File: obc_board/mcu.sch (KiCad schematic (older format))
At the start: 35 parts

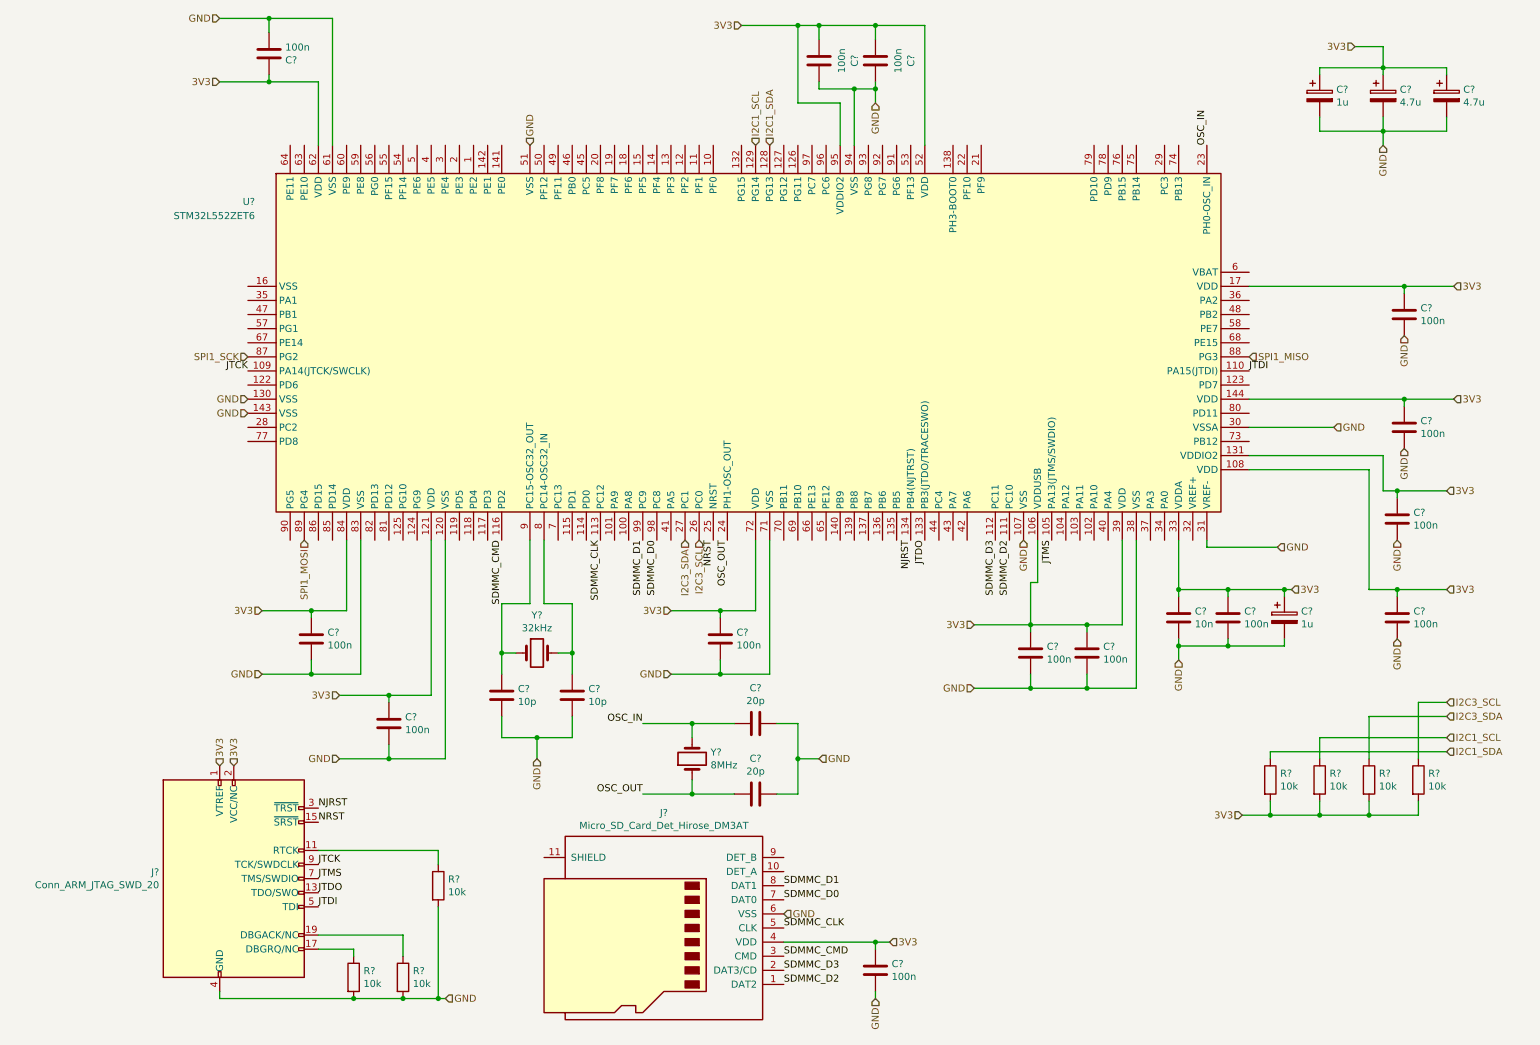
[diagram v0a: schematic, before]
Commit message: add memory
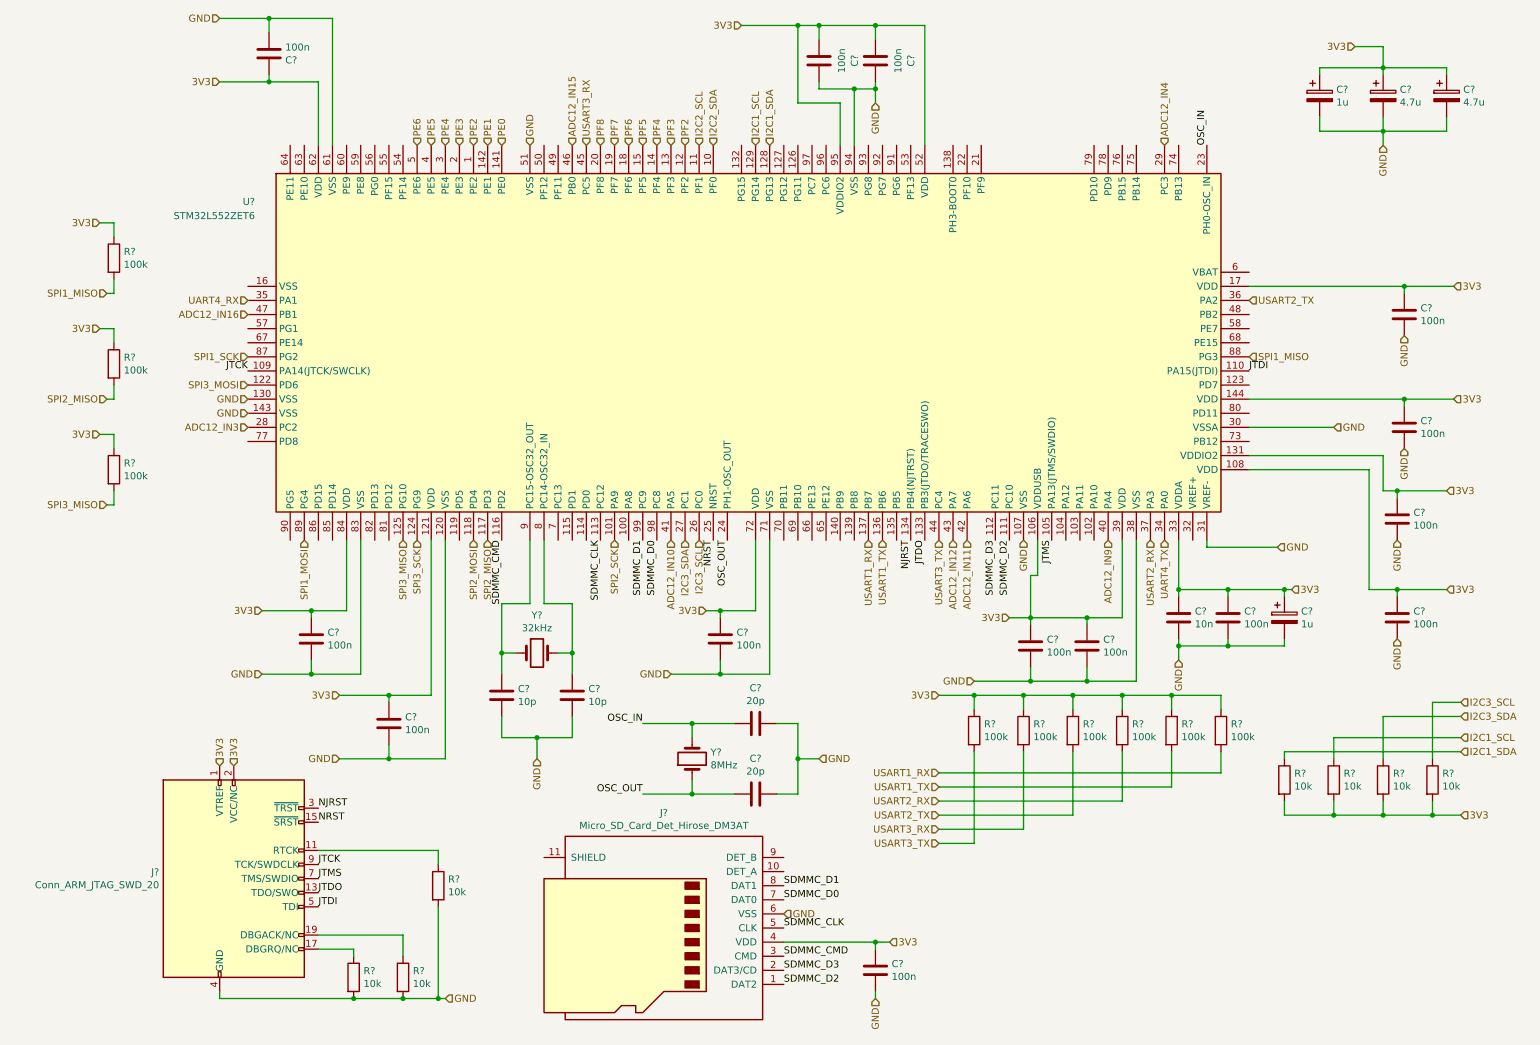
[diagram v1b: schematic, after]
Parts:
- added R? (x9): 100k, symbol Device:R
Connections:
- net 3V3: now also R?.1, R?.1, R?.1, R?.1, R?.1, R?.1, R?.1, R?.1, R?.1
- net SPI1_MISO: now also R?.2
- net PE2: now reaches U?.1 (PE2)
- net I2C2_SDA: now reaches U?.10 (PF0)
- net SPI2_SCK: now reaches U?.101 (PA9)
- net I2C2_SCL: now reaches U?.11 (PF1)
- net SPI2_MISO: now reaches U?.117 (PD3)
- net SPI2_MISO: now also R?.2
- net SPI2_MOSI: now reaches U?.118 (PD4)
- net PF2: now reaches U?.12 (PF2)
- net SPI3_MOSI: now reaches U?.122 (PD6)
- net SPI3_SCK: now reaches U?.124 (PG9)
- net SPI3_MISO: now reaches U?.125 (PG10)
- net SPI3_MISO: now also R?.2
- net PF3: now reaches U?.13 (PF3)
- net USART1_TX: now reaches U?.136 (PB6)
- net USART1_TX: now also R?.2
- net USART1_RX: now reaches U?.137 (PB7)
- net USART1_RX: now also R?.2
- net PF4: now reaches U?.14 (PF4)
- net PE0: now reaches U?.141 (PE0)
- net PE1: now reaches U?.142 (PE1)
- net PF5: now reaches U?.15 (PF5)
- net PF6: now reaches U?.18 (PF6)
- net PF7: now reaches U?.19 (PF7)
- net PE3: now reaches U?.2 (PE3)
- net PF8: now reaches U?.20 (PF8)
- net ADC12_IN3: now reaches U?.28 (PC2)
- net ADC12_IN4: now reaches U?.29 (PC3)
- net PE4: now reaches U?.3 (PE4)
- net UART4_TX: now reaches U?.34 (PA0)
- net UART4_RX: now reaches U?.35 (PA1)
- net USART2_TX: now reaches U?.36 (PA2)
- net USART2_TX: now also R?.2
- net USART2_RX: now reaches U?.37 (PA3)
- net USART2_RX: now also R?.2
- net PE5: now reaches U?.4 (PE5)
- net ADC12_IN9: now reaches U?.40 (PA4)
- net ADC12_IN10: now reaches U?.41 (PA5)
- net ADC12_IN11: now reaches U?.42 (PA6)
- net ADC12_IN12: now reaches U?.43 (PA7)
- net USART3_TX: now reaches U?.44 (PC4)
- net USART3_TX: now also R?.2
- net USART3_RX: now reaches U?.45 (PC5)
- net USART3_RX: now also R?.2
- net ADC12_IN15: now reaches U?.46 (PB0)
- net ADC12_IN16: now reaches U?.47 (PB1)
- net PE6: now reaches U?.5 (PE6)
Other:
- moved on the sheet: C?, R?

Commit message: updated footprints
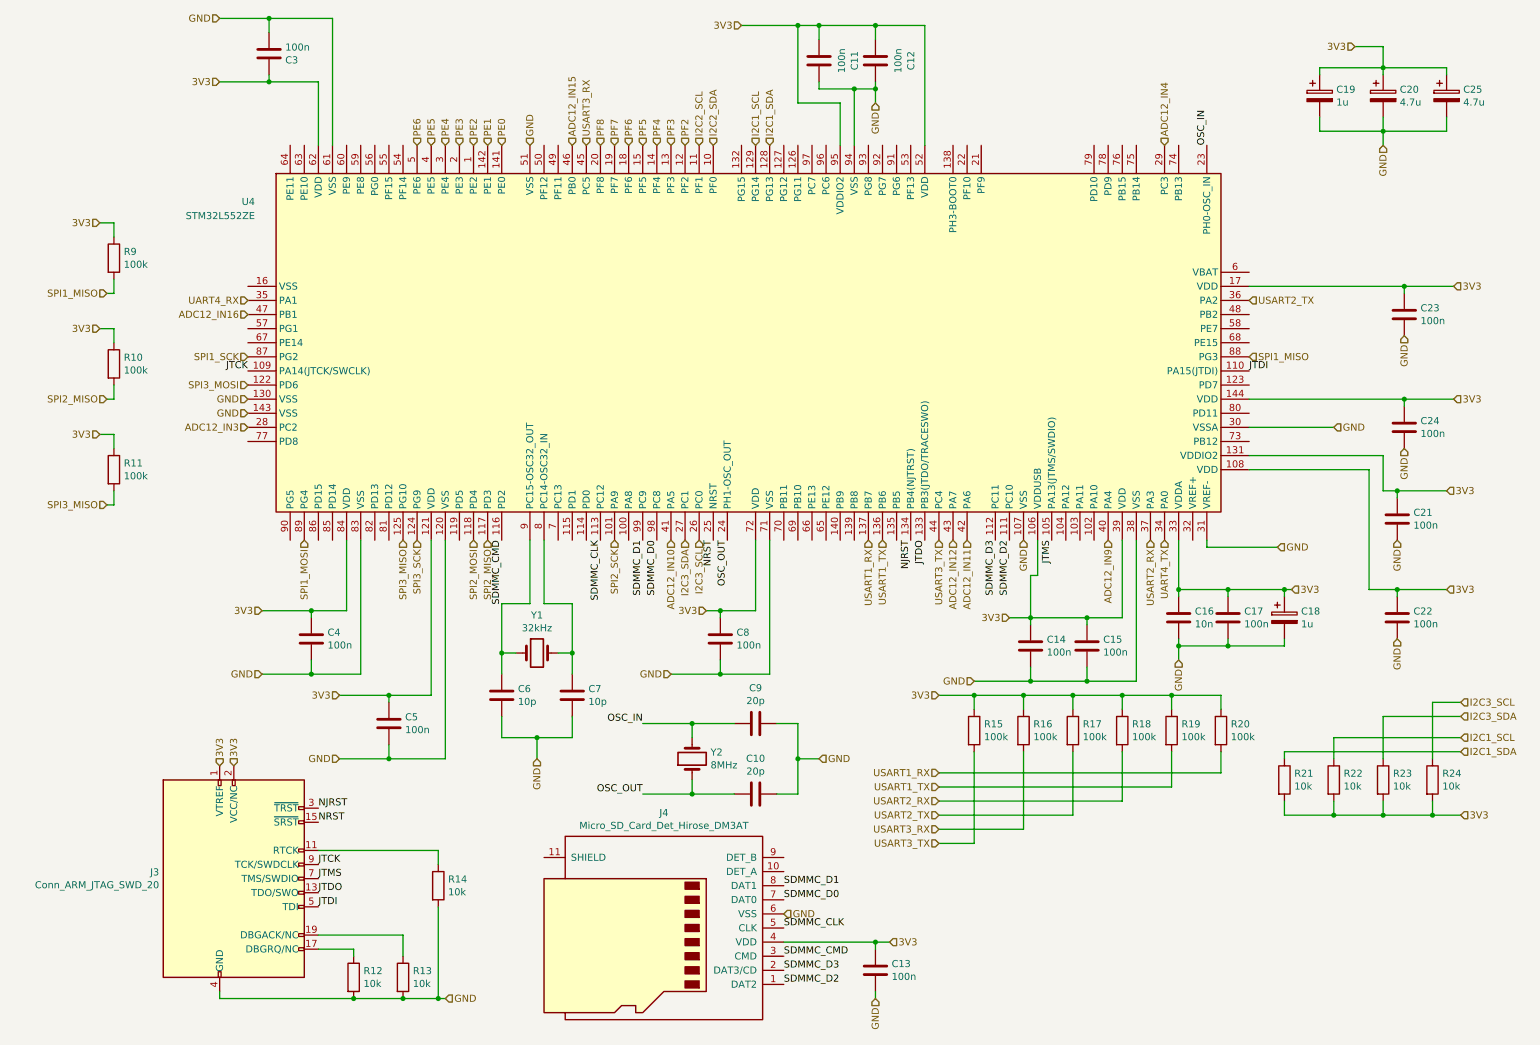
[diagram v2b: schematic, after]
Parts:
- C11, C12, C13, C14, C15, C17, C21, C22, C23, C24, C3, C4, C5, C8: renamed from C?; footprint (none) -> cubesat_obc:CAPC1005X55N; Digikey Part Number (none) -> 490-13342-1-ND
- C16: renamed from C?; footprint (none) -> cubesat_obc:CAPC0603X33N; Digikey Part Number (none) -> 490-6143-1-ND
- U4: renamed from U?; value STM32L552ZET6 -> STM32L552ZE; footprint Package_QFP:LQFP-144_20x20mm_P0.5mm -> cubesat_obc:LQFP-144_20x20mm_P0.5mm; Digikey Part Number (none) -> 497-STM32L552ZET6-ND
- gave numbers to parts that had none: 28

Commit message: footprints
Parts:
- C10, C9: footprint (none) -> Capacitor_SMD:C_0201_0603Metric; Digikey Part Number (none) -> 490-9618-1-ND
- C11, C12, C13, C14, C15, C17, C21, C22, C23, C24, C3, C4, C5, C8: footprint cubesat_obc:CAPC1005X55N -> Capacitor_SMD:C_0402_1005Metric; Digikey Part Number 490-13342-1-ND -> 490-16433-1-ND
- C16: footprint cubesat_obc:CAPC0603X33N -> Capacitor_SMD:C_0805_2012Metric; Digikey Part Number 490-6143-1-ND -> 490-8295-1-ND
- C18, C19: footprint (none) -> Capacitor_THT:CP_Radial_D5.0mm_P2.00mm; Digikey Part Number (none) -> 493-15407-ND
- C20, C25: footprint (none) -> Capacitor_THT:CP_Radial_D5.0mm_P2.00mm; Digikey Part Number (none) -> 493-15371-ND
- C6, C7: footprint (none) -> Capacitor_SMD:C_0201_0603Metric; Digikey Part Number (none) -> 490-7750-1-ND
- J3: footprint (none) -> Connector_IDC:IDC-Header_2x10_P2.54mm_Vertical
- J4: footprint (none) -> cubesat_obc:HRS_DM3AT-SF-PEJM5; Digikey Part Number (none) -> HR1964CT-ND
- R10, R11, R15, R16, R17, R18, R19, R20, R9: footprint (none) -> Resistor_SMD:R_0402_1005Metric; Digikey Part Number (none) -> 311-100KLRCT-ND
- R12, R13, R14, R21, R22, R23, R24: footprint (none) -> Resistor_SMD:R_0402_1005Metric; Digikey Part Number (none) -> 311-10.0KLRCT-ND

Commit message: expose more ios
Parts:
- removed J3: Conn_ARM_JTAG_SWD_20, Connector_IDC:IDC-Header_2x10_P2.54mm_Vertical, symbol Connector:Conn_ARM_JTAG_SWD_20
- removed J4: Micro_SD_Card_Det_Hirose_DM3AT, cubesat_obc:HRS_DM3AT-SF-PEJM5, symbol Connector:Micro_SD_Card_Det_Hirose_DM3AT
- removed R12, R13, R14: 10k, Resistor_SMD:R_0402_1005Metric, symbol Device:R
- added J4: Micro_SD_Card, cubesat_obc:microSD_HC_Wuerth_693072010801, symbol Connector:Micro_SD_Card
- added J?: Conn_01x08_Female, symbol Connector:Conn_01x08_Female
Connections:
- net 3V3: now also J?.8 (Pin_8)
- net GND: now also J4.6 (VSS), J4.9 (SHIELD), J?.7 (Pin_7)
- net JTCK: now also J?.4 (Pin_4)
- net JTDI: now also J?.1 (Pin_1)
- net JTDO: now also J?.2 (Pin_2)
- net JTMS: now also J?.3 (Pin_3)
- net NJRST: now also J?.6 (Pin_6)
- net NRST: now also J?.5 (Pin_5)
- net SDMMC_CLK: now also J4.5 (CLK)
- net SDMMC_CMD: now also J4.3 (CMD)
- net SDMMC_D0: now also J4.7 (DAT0)
- net SDMMC_D1: now also J4.8 (DAT1)
- net SDMMC_D2: now also J4.1 (DAT2)
- net SDMMC_D3: now also J4.2 (DAT3/CD)
- net 3V3_P: now reaches U4.6 (VBAT)
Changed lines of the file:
@@
 $Descr A4 11693 8268
 encoding utf-8
-Sheet 3 5
+Sheet 3 6
 Title ""
 Date ""
@@
 Wire Wire Line
 	5250 6100 5550 6100
-$Comp
-L Connector:Conn_ARM_JTAG_SWD_20 J3
-U 1 1 5E8B9B17
-P 2000 6700
-F 0 "J3" H 1471 6746 50  0000 R CNN
-F 1 "Conn_ARM_JTAG_SWD_20" H 1471 6655 50  0000 R CNN
-F 2 "Connector_IDC:IDC-Header_2x10_P2.54mm_Vertical" H 2450 5650 50  0001 L TNN
-F 3 "http://infocenter.arm.com/help/topic/com.arm.doc.dui0499b/DUI0499B_system_design_reference.pdf" V 1650 5450 50  0001 C CNN
-	1    2000 6700
-	1    0    0    -1
-$EndComp
-Text HLabel 1900 5900 1    50   Input ~ 0
-3V3
-Text HLabel 2000 5900 1    50   Input ~ 0
-3V3
-Text HLabel 3500 7550 2    50   Input ~ 0
-GND
-Wire Wire Line
-	1900 7550 1900 7500
-Wire Wire Line
-	1900 7550 2850 7550
-$Comp
-L Device:R R12
-U 1 1 5E922293
-P 2850 7400
-F 0 "R12" H 2920 7446 50  0000 L CNN
-F 1 "10k" H 2920 7355 50  0000 L CNN
-F 2 "Resistor_SMD:R_0402_1005Metric" V 2780 7400 50  0001 C CNN
-F 3 "https://www.yageo.com/upload/media/product/productsearch/datasheet/rchip/PYu-RC_Group_51_RoHS_L_11.pdf~" H 2850 7400 50  0001 C CNN
-F 4 "311-10.0KLRCT-ND" H 2850 7400 50  0001 C CNN "Digikey Part Number"
-	1    2850 7400
-	1    0    0    -1
-$EndComp
-Connection ~ 2850 7550
-Wire Wire Line
-	2850 7550 3200 7550
-$Comp
-L Device:R R13
-U 1 1 5E922EFC
-P 3200 7400
-F 0 "R13" H 3270 7446 50  0000 L CNN
-F 1 "10k" H 3270 7355 50  0000 L CNN
-F 2 "Resistor_SMD:R_0402_1005Metric" V 3130 7400 50  0001 C CNN
-F 3 "https://www.yageo.com/upload/media/product/productsearch/datasheet/rchip/PYu-RC_Group_51_RoHS_L_11.pdf~" H 3200 7400 50  0001 C CNN
-F 4 "311-10.0KLRCT-ND" H 3200 7400 50  0001 C CNN "Digikey Part Number"
-	1    3200 7400
-	1    0    0    -1
-$EndComp
-Wire Wire Line
-	2600 7200 2850 7200
-Wire Wire Line
-	2850 7200 2850 7250
-$Comp
-L Device:R R14
-U 1 1 5E92F679
-P 3450 6750
-F 0 "R14" H 3520 6796 50  0000 L CNN
-F 1 "10k" H 3520 6705 50  0000 L CNN
-F 2 "Resistor_SMD:R_0402_1005Metric" V 3380 6750 50  0001 C CNN
-F 3 "https://www.yageo.com/upload/media/product/productsearch/datasheet/rchip/PYu-RC_Group_51_RoHS_L_11.pdf~" H 3450 6750 50  0001 C CNN
-F 4 "311-10.0KLRCT-ND" H 3450 6750 50  0001 C CNN "Digikey Part Number"
-	1    3450 6750
-	1    0    0    -1
-$EndComp
-Connection ~ 3200 7550
-Wire Wire Line
-	3200 7550 3450 7550
-Wire Wire Line
-	3200 7250 3200 7100
-Wire Wire Line
-	3200 7100 2600 7100
-Wire Wire Line
-	3450 6900 3450 7550
-Connection ~ 3450 7550
-Wire Wire Line
-	3450 7550 3500 7550
-Wire Wire Line
-	3450 6600 3450 6500
-Wire Wire Line
-	3450 6500 2600 6500
+Text HLabel 1800 6500 2    50   Input ~ 0
+3V3
 Text HLabel 8700 5150 3    50   Input ~ 0
 GND
@@
 Text Label 4900 6100 2    50   ~ 0
 OSC_OUT
-Text Label 2600 6900 0    50   ~ 0
+Text Label 1800 7200 0    50   ~ 0
 JTDI
-Text Label 2600 6800 0    50   ~ 0
+Text Label 1800 7100 0    50   ~ 0
 JTDO
-Text Label 2600 6700 0    50   ~ 0
+Text Label 1800 7000 0    50   ~ 0
 JTMS
-Text Label 2600 6600 0    50   ~ 0
+Text Label 1800 6900 0    50   ~ 0
 JTCK
-Text Label 2600 6200 0    50   ~ 0
+Text Label 1800 6700 0    50   ~ 0
 NJRST
-Text Label 2600 6300 0    50   ~ 0
+Text Label 1800 6800 0    50   ~ 0
 NRST
 Wire Wire Line
@@
 Text HLabel 5200 4300 3    50   Input ~ 0
 I2C3_SDA
-$Comp
-L Connector:Micro_SD_Card_Det_Hirose_DM3AT J4
-U 1 1 5F6001BE
-P 5000 7050
-F 0 "J4" H 4950 6233 50  0000 C CNN
-F 1 "Micro_SD_Card_Det_Hirose_DM3AT" H 4950 6324 50  0000 C CNN
-F 2 "cubesat_obc:HRS_DM3AT-SF-PEJM5" H 7050 7750 50  0001 C CNN
-F 3 "https://www.hirose.com/product/document?clcode=CL0609-0033-6-00&productname=DM3AT-SF-PEJ2M5&series=DM3&documenttype=Catalog&lang=en&documentid=D49662_en" H 5000 7150 50  0001 C CNN
-F 4 "HR1964CT-ND" H 5000 7050 50  0001 C CNN "Digikey Part Number"
-	1    5000 7050
-	-1   0    0    1
-$EndComp
 Connection ~ 2250 600
 Wire Wire Line
@@
 Text Label 4600 4300 3    50   ~ 0
 SDMMC_CLK
-Text Label 5900 6850 0    50   ~ 0
+Text Label 4550 6700 0    50   ~ 0
 SDMMC_D0
-Text Label 5900 6750 0    50   ~ 0
+Text Label 4550 6600 0    50   ~ 0
 SDMMC_D1
-Text Label 5900 7450 0    50   ~ 0
+Text Label 4550 7300 0    50   ~ 0
 SDMMC_D2
-Text Label 5900 7350 0    50   ~ 0
+Text Label 4550 7200 0    50   ~ 0
 SDMMC_D3
-Text Label 5900 7250 0    50   ~ 0
+Text Label 4550 7100 0    50   ~ 0
 SDMMC_CMD
-Text Label 5900 7050 0    50   ~ 0
+Text Label 4550 6900 0    50   ~ 0
 SDMMC_CLK
 Text HLabel 6650 7150 2    50   Input ~ 0
 3V3
 Wire Wire Line
-	5900 7150 6550 7150
+	4550 7000 5200 7000
 $Comp
 L Device:R R22
@@
 Wire Wire Line
 	6550 7150 6550 7200
-Connection ~ 6550 7150
 Wire Wire Line
 	6550 7150 6650 7150
-Text HLabel 5900 6950 2    50   Input ~ 0
+Text HLabel 4550 6800 2    50   Input ~ 0
 GND
 Wire Wire Line
@@
 	5350 4800 5450 4800
 Connection ~ 5450 4800
+$Comp
+L Connector:Micro_SD_Card J4
+U 1 1 5F37C195
+P 3650 7000
+F 0 "J4" H 3600 6183 50  0000 C CNN
+F 1 "Micro_SD_Card" H 3600 6274 50  0000 C CNN
+F 2 "cubesat_obc:microSD_HC_Wuerth_693072010801" H 4800 7300 50  0001 C CNN
+F 3 "http://katalog.we-online.de/em/datasheet/693072010801.pdf" H 3650 7000 50  0001 C CNN
+F 4 "732-3820-6-ND" H 3650 7000 50  0001 C CNN "Digikey Part Number"
+	1    3650 7000
+	-1   0    0    1
+$EndComp
+Text HLabel 2850 6400 0    50   Input ~ 0
+GND
+$Comp
+L Connector:Conn_01x08_Female J?
+U 1 1 5F3C5B25
+P 1600 6900
+F 0 "J?" H 1492 6275 50  0000 C CNN
+F 1 "Conn_01x08_Female" H 1492 6366 50  0000 C CNN
+F 2 "" H 1600 6900 50  0001 C CNN
+F 3 "~" H 1600 6900 50  0001 C CNN
+	1    1600 6900
+	-1   0    0    1
+$EndComp
+Text HLabel 1800 6600 2    50   Input ~ 0
+GND
+Text HLabel 9200 2400 2    50   Input ~ 0
+3V3_P
 $EndSCHEMATC

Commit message: footprints
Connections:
- net PG6: now reaches U4.91 (PG6)
- net PG7: now reaches U4.92 (PG7)
- net PG8: now reaches U4.93 (PG8)
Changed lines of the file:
@@
 Wire Wire Line
 	6550 750  6550 650
-Text HLabel 6550 1200 3    50   Input ~ 0
+Text HLabel 6650 1100 2    50   Input ~ 0
 GND
 $Comp
@@
 	6150 1100 6400 1100
 Connection ~ 6550 1100
-Wire Wire Line
-	6550 1100 6550 1200
 Wire Wire Line
 	6400 1100 6400 1500
@@
 Text HLabel 9200 2400 2    50   Input ~ 0
 3V3_P
+Text HLabel 6700 1500 1    50   Input ~ 0
+PG6
+Text HLabel 6600 1500 1    50   Input ~ 0
+PG7
+Wire Wire Line
+	6550 1100 6650 1100
+Text HLabel 6500 1500 1    50   Input ~ 0
+PG8
 $EndSCHEMATC

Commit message: pcb layout
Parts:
- C18, C19: footprint Capacitor_THT:CP_Radial_D5.0mm_P2.00mm -> Capacitor_SMD:CP_Elec_4x5.3; Digikey Part Number 493-15407-ND -> 565-2486-1-ND
- C20, C25: footprint Capacitor_THT:CP_Radial_D5.0mm_P2.00mm -> Capacitor_SMD:CP_Elec_4x5.3; Digikey Part Number 493-15371-ND -> 565-2471-1-ND
- J8: renamed from J?; footprint (none) -> Connector_Molex:Molex_PicoBlade_53261-0871_1x08-1MP_P1.25mm_Horizontal; Digikey Part Number (none) -> WM7626CT-ND
- renumbered J4 to J9, R15 to R12, R16 to R13, R17 to R14, R18 to R15, R19 to R16, R20 to R17, R21 to R18, R22 to R19, R23 to R20, R24 to R21, U4 to U3
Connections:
- net 3V3: now also J9.4 (VDD)
- net I2C1_SCL: no longer R19.1
- net I2C1_SDA: no longer R18.1
- net I2C2_SCL: now also R19.1
- net I2C2_SDA: now also R18.1
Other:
- moved on the sheet: C13
